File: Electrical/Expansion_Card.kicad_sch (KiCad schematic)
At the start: 15 parts, among them J1 SJ-3501-SMT-TR, J2 SJ-3501-SMT-TR, P1 USB_C_Plug_USB2.0, U1 AP2112K-3.3, U2 PCM2906, U3 TPA6132A2RTE

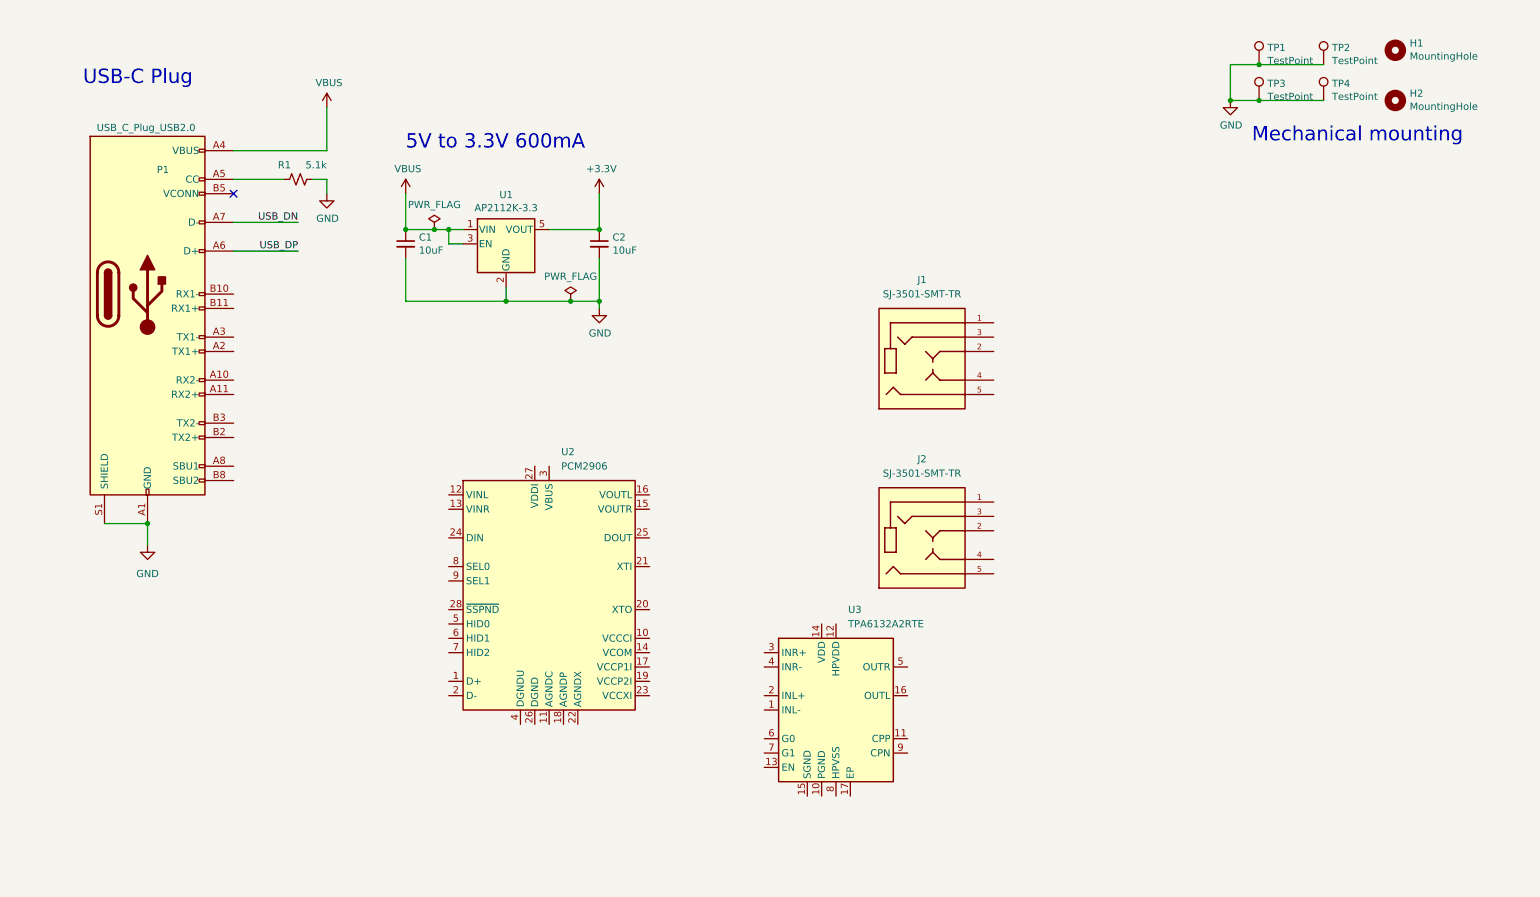
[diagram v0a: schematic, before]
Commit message: New footprints and components added
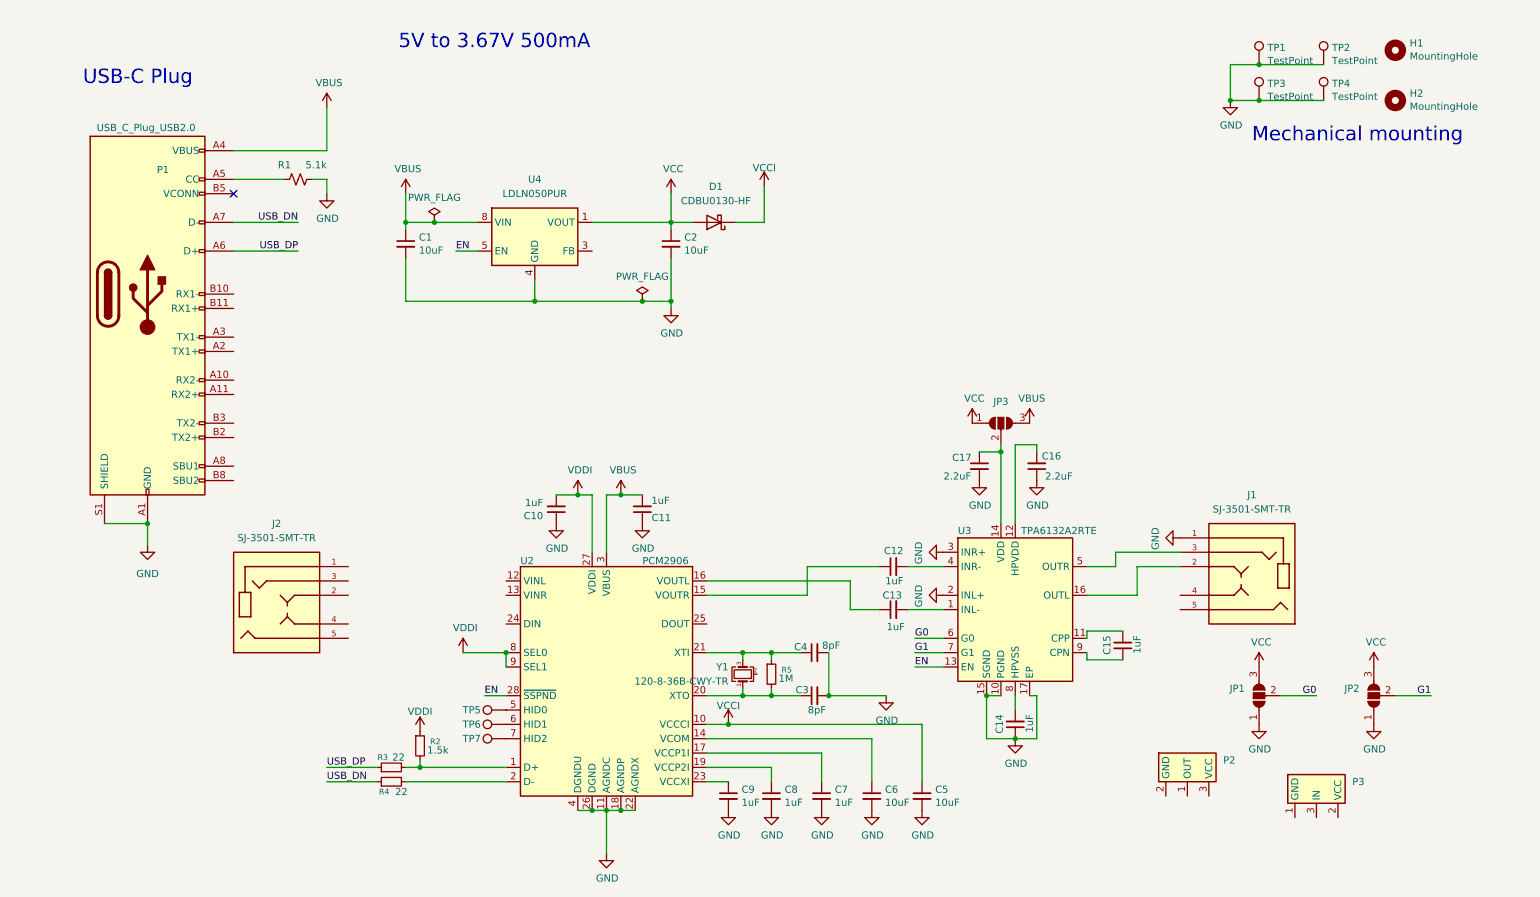
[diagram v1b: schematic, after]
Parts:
- removed U1: AP2112K-3.3, Package_TO_SOT_SMD:SOT-23-5, symbol Regulator_Linear:AP2112K-3.3
- added C10, C11, C12, C13, C14, C15, C7, C8, C9: 1uF, Capacitor_SMD:C_0402_1005Metric, symbol Device:C_Small
- added C16, C17: 2.2uF, Capacitor_SMD:C_0402_1005Metric, symbol Device:C_Small
- added C3, C4: 8pF, Capacitor_SMD:C_0402_1005Metric, symbol Device:C_Small
- added C5, C6: 10uF, Capacitor_SMD:C_0402_1005Metric, symbol Device:C_Small
- added D1: CDBU0130-HF, Diode_SMD:D_SOD-523, symbol Diode:CDBU40-HF
- added JP1, JP2, JP3: SolderJumper_3_Open, Jumper:SolderJumper-3_P1.3mm_Open_RoundedPad1.0x1.5mm, symbol Jumper:SolderJumper_3_Open
- added P2: ~, Expansion_Card:TX_RX_module, symbol Optical_transmitter_receiver:Receiver
- added P3: ~, Expansion_Card:TX_RX_module, symbol Optical_transmitter_receiver:Transmitter
- added R2: 1.5k, Resistor_SMD:R_0402_1005Metric, symbol Device:R_Small
- added R3, R4: 22, Resistor_SMD:R_0402_1005Metric, symbol Device:R_Small
- added R5: 1M, Resistor_SMD:R_0402_1005Metric, symbol Device:R_Small
- added TP5, TP6, TP7: TestPoint, TestPoint:TestPoint_Pad_D1.0mm, symbol Connector:TestPoint
- added U4: LDLN050PUR, Package_DFN_QFN:DFN-8-1EP_3x3mm_P0.65mm_EP1.55x2.4mm, symbol LDLN050:LDLN050PUR
- added Y1: 120-8-36B-CWY-TR, Crystal:Crystal_SMD_2520-4Pin_2.5x2.0mm, symbol Device:Crystal_GND24_Small
- C1, C2: footprint Capacitor_SMD:C_0805_2012Metric -> Capacitor_SMD:C_0402_1005Metric
- R1: footprint Resistor_SMD:R_0603_1608Metric -> Resistor_SMD:R_0402_1005Metric
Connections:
- net GND: now also J1.1, U2.11 (AGNDC), U2.18 (AGNDP), U2.22 (AGNDX), U2.26 (DGND), U2.4 (DGNDU), U3.10 (PGND), U3.15 (SGND), U3.17 (EP), U3.2 (INL+), U3.3 (INR+), C10.1, C11.1, C14.1, C16.1, C17.2, C3.2, C4.2, C5.2, C6.2, C7.2, C8.2, C9.2, JP1.1 (A), JP2.1 (A), U4.4 (GND), U4.9 (GND)
- net USB_DN: now also R4.1
- net USB_DP: now also R3.1
- net VBUS: now also U2.3 (VBUS), C11.2, JP3.3 (B), U4.8 (VIN)
- net at J1.2: now also U3.16 (OUTL)
- net at J1.3: now also U3.5 (OUTR)
- net at U2.1 (D+): now also R2.2, R3.2
- net VCCI: now reaches U2.10 (VCCCI)
- net VCCI: now also C5.1, D1.1 (K)
- net at U2.14 (VCOM): now also C6.1
- net at U2.15 (VOUTR): now also C12.1
- net at U2.16 (VOUTL): now also C13.1
- net at U2.17 (VCCP1I): now also C7.1
- net at U2.19 (VCCP2I): now also C8.1
- net at U2.2 (D-): now also R4.2
- net at U2.20 (XTO): now also C3.1, R5.2, Y1.1
- net at U2.21 (XTI): now also C4.1, R5.1, Y1.3
- net at U2.23 (VCCXI): now also C9.1
- net VDDI: now reaches U2.27 (VDDI)
- net VDDI: now also U2.8 (SEL0), U2.9 (SEL1), C10.2, R2.1
- net EN: now reaches U2.28 (~{SSPND})
- net EN: now also U3.13 (EN), U4.5 (EN)
- net at U2.5 (HID0): now also TP5.1
- net at U2.6 (HID1): now also TP6.1
- net at U2.7 (HID2): now also TP7.1
- net at U3.1 (INL-): now also C13.2
- net at U3.11 (CPP): now also C15.2
- net at U3.12 (HPVDD): now also C16.2
- net at U3.14 (VDD): now also C17.1, JP3.2 (C)
- net at U3.4 (INR-): now also C12.2
- net G0: now reaches U3.6 (G0)
- net G0: now also JP1.2 (C)
- net G1: now reaches U3.7 (G1)
- net G1: now also JP2.2 (C)
- net at U3.8 (HPVSS): now also C14.2
- net at U3.9 (CPN): now also C15.1
- net +3.3V renamed VCC
- net VCC: now also D1.2 (A), JP1.3 (B), JP2.3 (B), JP3.1 (A), U4.1 (VOUT)
- new net: U4.2 (NC), U4.6 (NC), U4.7 (NC)
- new net: Y1.2 (G), Y1.4 (G)
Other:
- note added: "5V to 3.67V 500mA"
- note removed: "5V to 3.3V 600mA"
- moved on the sheet: C2, J1, J2, U2, U3

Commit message: Schematic completed + basic layout
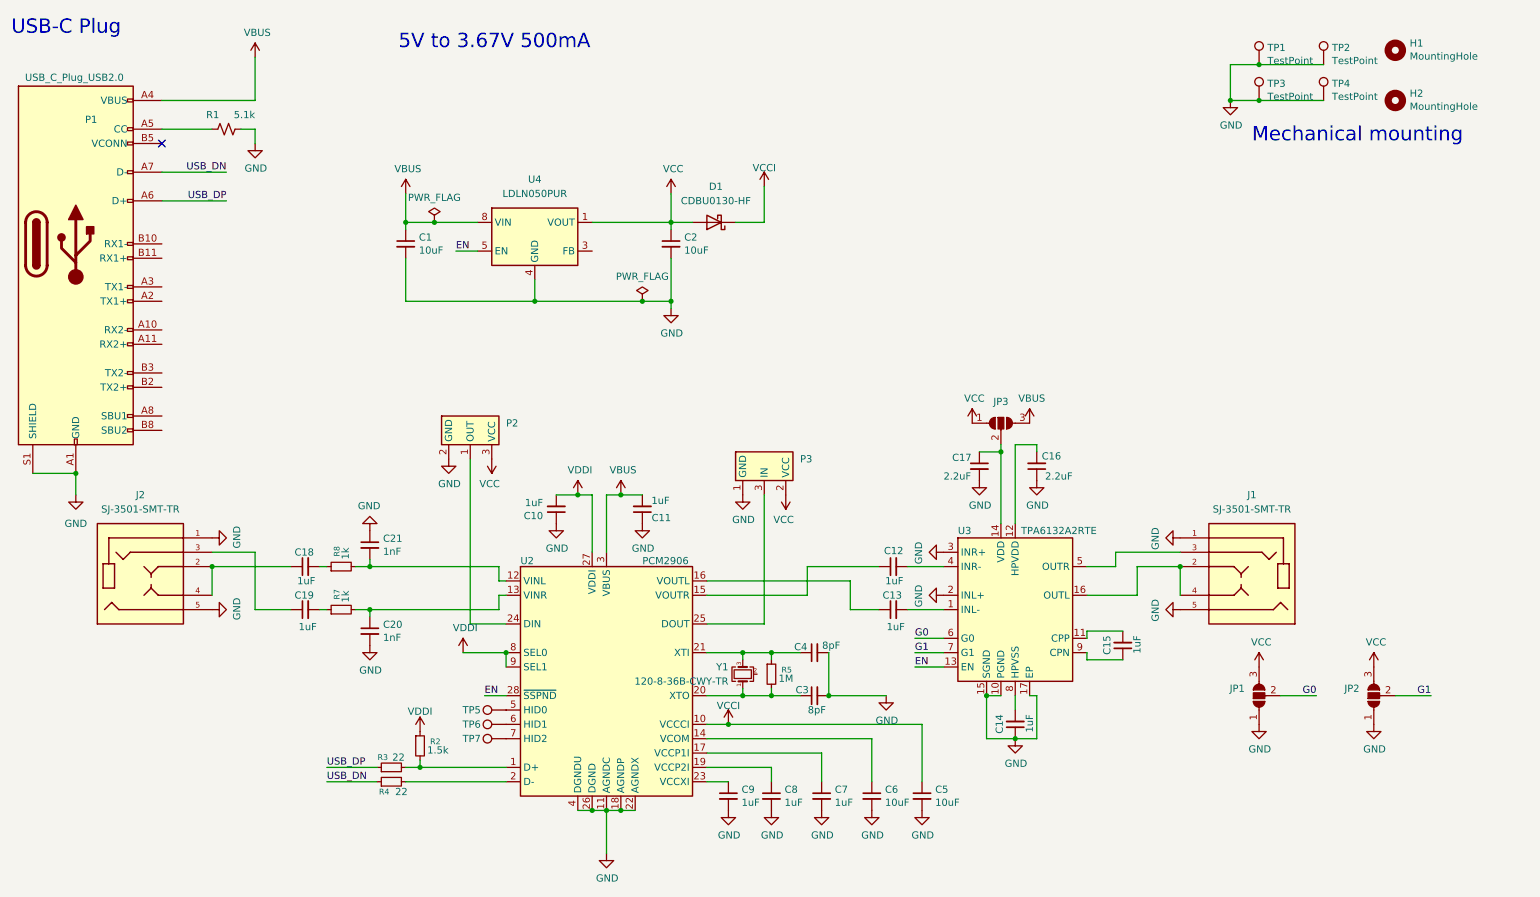
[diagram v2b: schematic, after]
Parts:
- added C18, C19: 1uF, Capacitor_SMD:C_0402_1005Metric, symbol Device:C_Small
- added C20, C21: 1nF, Capacitor_SMD:C_0402_1005Metric, symbol Device:C_Small
- added R7, R8: 1k, Resistor_SMD:R_0402_1005Metric, symbol Device:R_Small
- JP1, JP2, JP3: footprint Jumper:SolderJumper-3_P1.3mm_Open_RoundedPad1.0x1.5mm -> Expansion_Card:Jumper_small_straight
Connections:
- net GND: now also J1.5, J2.1, J2.5, P2.2 (GND), P3.1 (GND), C20.2, C21.1
- net VCC: now also P2.3 (VCC), P3.2 (VCC)
- net at J1.2, U3.16 (OUTL): now also J1.4
- net at P3.3 (IN): now also U2.25 (DOUT)
- net at U2.12 (VINL): now also C21.2, R8.2
- net at U2.13 (VINR): now also C20.1, R7.2
- net at U2.24 (DIN): now also P2.1 (OUT)
- net at J2.2: now also J2.4, C18.1
- net at J2.3: now also C19.1
- new net: C18.2, R8.1
- new net: C19.2, R7.1
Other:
- moved on the sheet: J2, P1, P2, P3, R1

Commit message: Routing + output
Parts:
- removed TP1, TP2, TP3, TP4: TestPoint, TestPoint:TestPoint_Pad_1.5x1.5mm, symbol Connector:TestPoint
- added P4: ~, Expansion_Card:TX_RX_module, symbol Optical_transmitter_receiver:Transmitter
- added P5: ~, Expansion_Card:TX_RX_module, symbol Optical_transmitter_receiver:Receiver
- added R6: 150k, Resistor_SMD:R_0402_1005Metric, symbol Device:R_Small
- added R9: 300k, Resistor_SMD:R_0402_1005Metric, symbol Device:R_Small
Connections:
- net GND: now also Y1.2 (G), Y1.4 (G), P4.1 (GND), P5.2 (GND), R6.1
- net VCC: now also P4.2 (VCC), P5.3 (VCC), R9.2
- net at C18.1, J2.4: no longer J2.2
- net at J1.4, U3.16 (OUTL): no longer J1.2
- net at P3.3 (IN), U2.25 (DOUT): now also P4.3 (IN)
- net at P2.1 (OUT), U2.24 (DIN): now also P5.1 (OUT)
- net at U4.3 (FB): now also R6.2, R9.1
- no-connect marks 1 -> 13
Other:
- moved on the sheet: P2, R5, Y1
